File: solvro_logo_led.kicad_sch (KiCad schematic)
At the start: 0 parts

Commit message: Zmiana zasilania na 4.5V
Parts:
- added BT1: 4.5V Battery, symbol Device:Battery
- added C1, C2: 100nF, symbol Device:C
- added C3: 10uF, symbol Device:C
- added D1, D10, D11, D12, D13, D14, D15, D16, D17, D18, D19, D2, D20, D21, D22, D23, D24, D25, D26, D3, D4, D5, D6, D7, D8, D9: LED, symbol Device:LED
- added R1, R2, R3, R4, R5, R6: 47R, symbol Device:R
- added R7: 10K, symbol Device:R
- added U1: ATmega328-P, Package_DIP:DIP-28_W7.62mm, symbol MCU_Microchip_ATmega:ATmega328-P
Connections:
- new net: D15.2 (A), D16.1 (K), D21.2 (A), D22.1 (K), D25.2 (A), D26.1 (K), D5.2 (A), D6.1 (K), D7.1 (K), D8.2 (A), R5.2
- new net: D1.1 (K), D10.1 (K), D13.1 (K), D14.2 (A), D2.2 (A), D21.1 (K), D22.2 (A), D9.2 (A), R2.2
- new net: D17.2 (A), D18.1 (K), D23.2 (A), D24.1 (K), D7.2 (A), D8.1 (K), R6.2
- new net: R7.2, U1.1 (~{RESET}/PC6)
- new net: BT1.1 (+), C2.1, C3.1, R7.1, U1.20 (AVCC), U1.7 (VCC)
- new net: C1.1, U1.21 (AREF)
- new net: BT1.2 (-), C1.2, C2.2, C3.2, U1.22 (GND), U1.8 (GND)
- new net: D10.2 (A), D11.1 (K), D12.2 (A), D19.1 (K), D20.2 (A), D25.1 (K), D26.2 (A), D9.1 (K), R1.2
- new net: D1.2 (A), D11.2 (A), D12.1 (K), D15.1 (K), D16.2 (A), D2.1 (K), D23.1 (K), D24.2 (A), D3.1 (K), D4.2 (A), R3.2
- new net: D13.2 (A), D14.1 (K), D17.1 (K), D18.2 (A), D19.2 (A), D20.1 (K), D3.2 (A), D4.1 (K), D5.1 (K), D6.2 (A), R4.2
- new net A: R1.1, U1.4 (PD2)
- new net B: R2.1, U1.5 (PD3)
- new net C: R3.1, U1.6 (PD4)
- new net D: R4.1, U1.11 (PD5)
- new net E: R5.1, U1.12 (PD6)
- new net F: R6.1, U1.13 (PD7)
- no-connect marks 0 -> 16

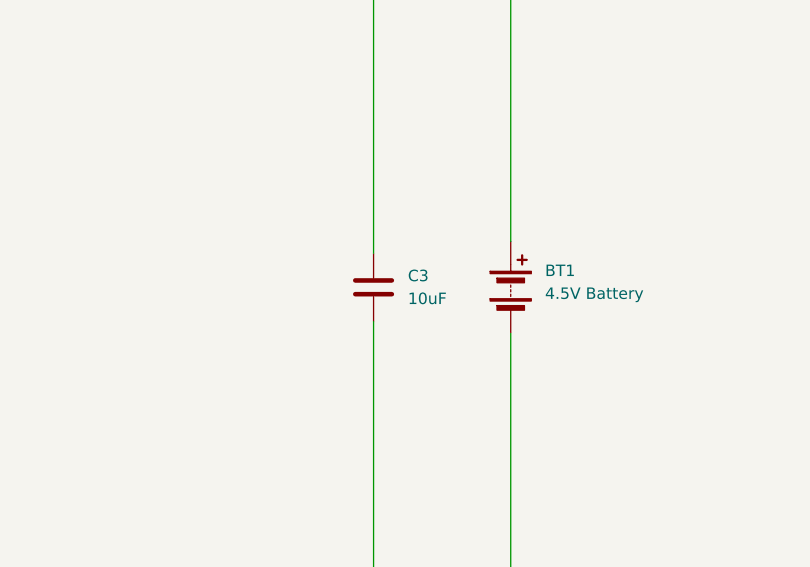
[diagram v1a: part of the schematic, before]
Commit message: Dodanie plików gerber, schematu, płytki produkcyjnej i stp
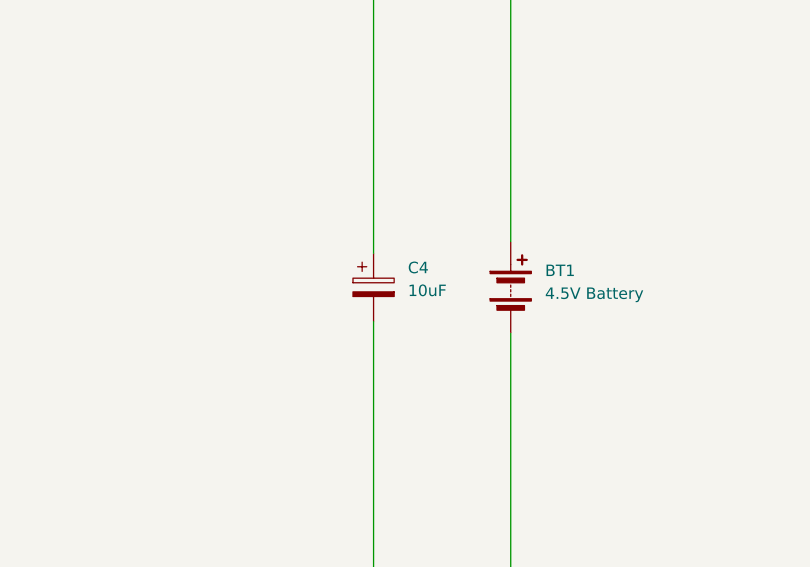
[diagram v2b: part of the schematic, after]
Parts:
- removed C3: 10uF, symbol Device:C
- added C4: 10uF, Capacitor_SMD:C_1206_3216Metric_Pad1.33x1.80mm_HandSolder, symbol Device:C_Polarized
- BT1: footprint (none) -> Battery:BatteryHolder_Keystone_2479_3xAAA
- C1, C2: footprint (none) -> Capacitor_SMD:C_1206_3216Metric_Pad1.33x1.80mm_HandSolder
- D1, D10, D11, D12, D13, D14, D15, D16, D17, D18, D19, D2, D20, D21, D22, D23, D24, D25, D26, D3, D4, D5, D6, D7, D8, D9: footprint (none) -> LED_SMD:LED_1206_3216Metric_Pad1.42x1.75mm_HandSolder
- R1, R2, R3, R4, R5, R6, R7: footprint (none) -> Resistor_SMD:R_1206_3216Metric_Pad1.30x1.75mm_HandSolder
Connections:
- net at BT1.1 (+), C2.1, R7.1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: now also C4.1
- net at BT1.2 (-), C1.2, C2.2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: now also C4.2
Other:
- company: (none) -> Michał Bocian
- title: (none) -> Solvro Logo LED
